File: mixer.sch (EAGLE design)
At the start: 49 parts, among them U1 MAX5419LETA+, U2 MAX5419LETA+, X1 OPAMP, X10 OPAMP, X3 OPAMP, X5 OPAMP, X6 OPAMP, X7 OPAMP, X8 OPAMP, X9 OPAMP

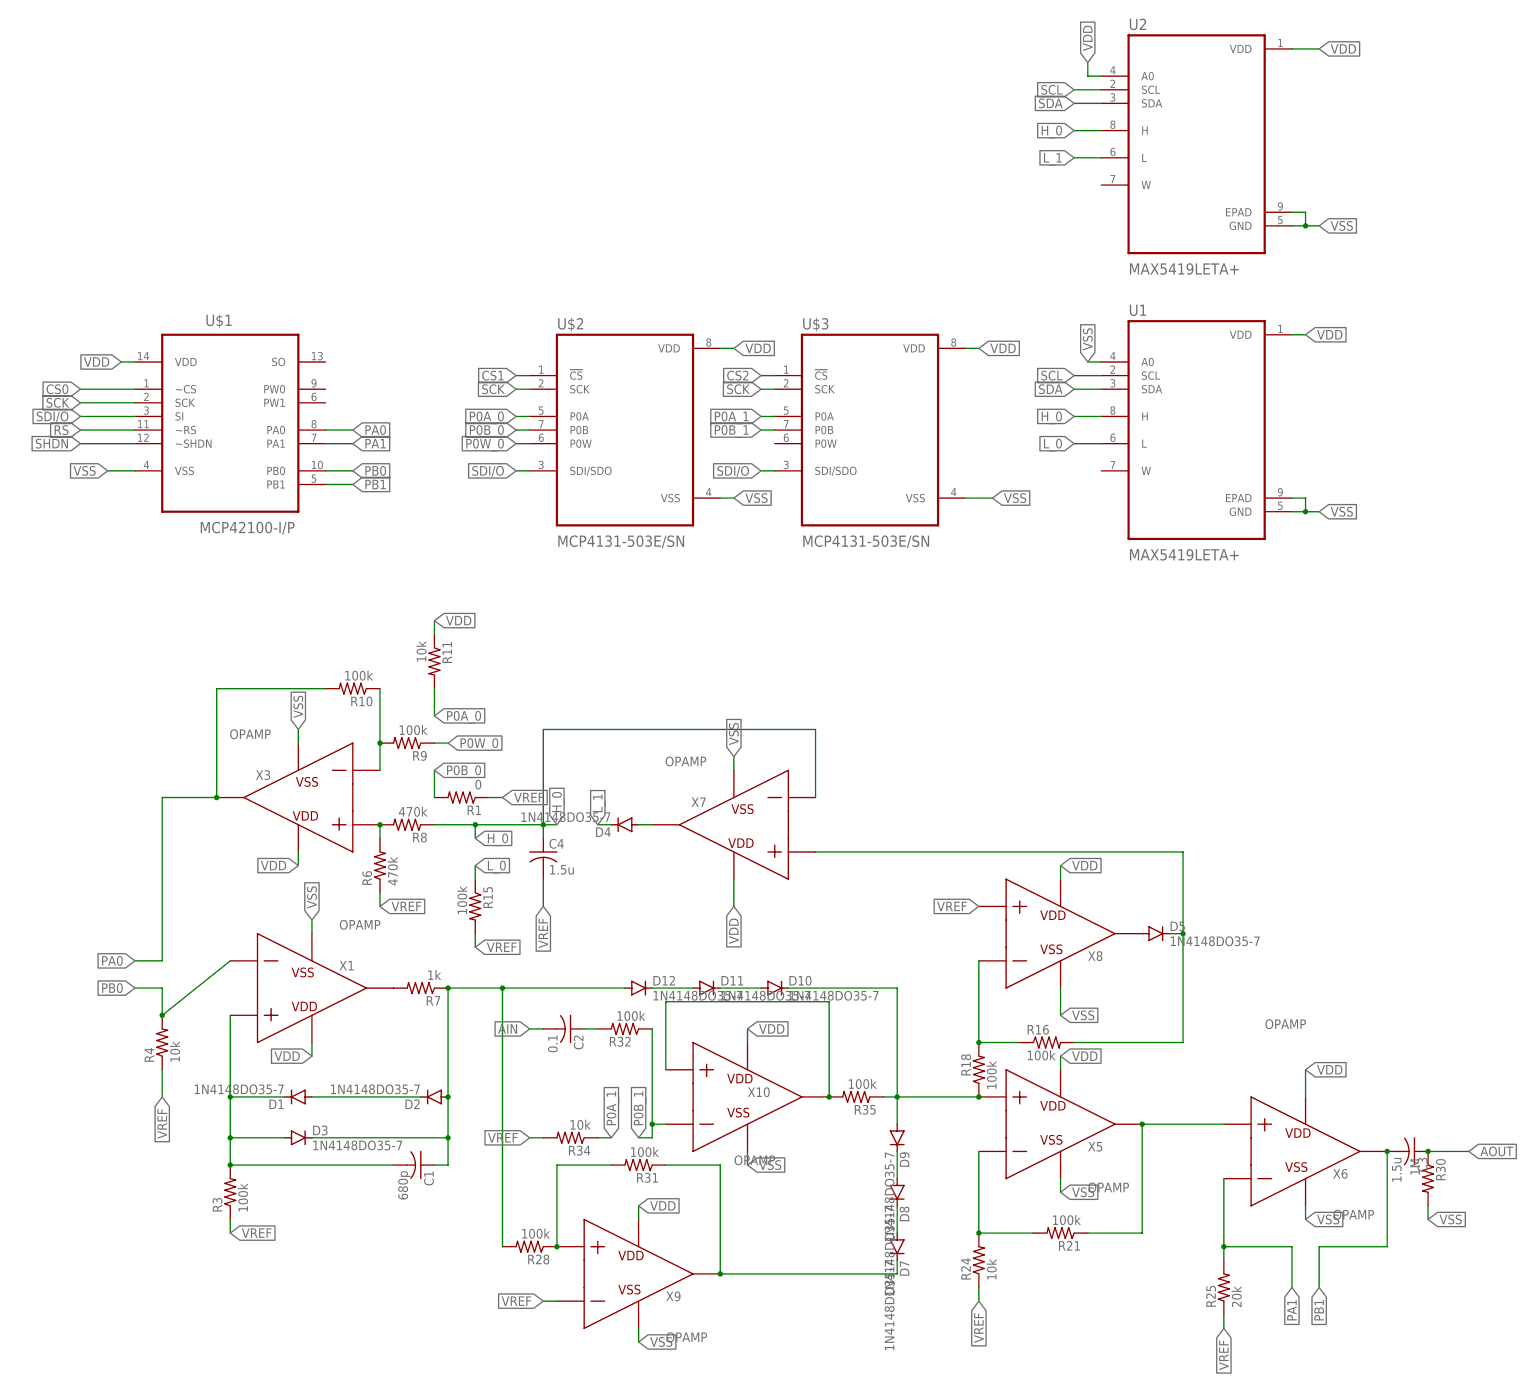
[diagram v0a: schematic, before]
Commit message: update, split out into schematics for each component
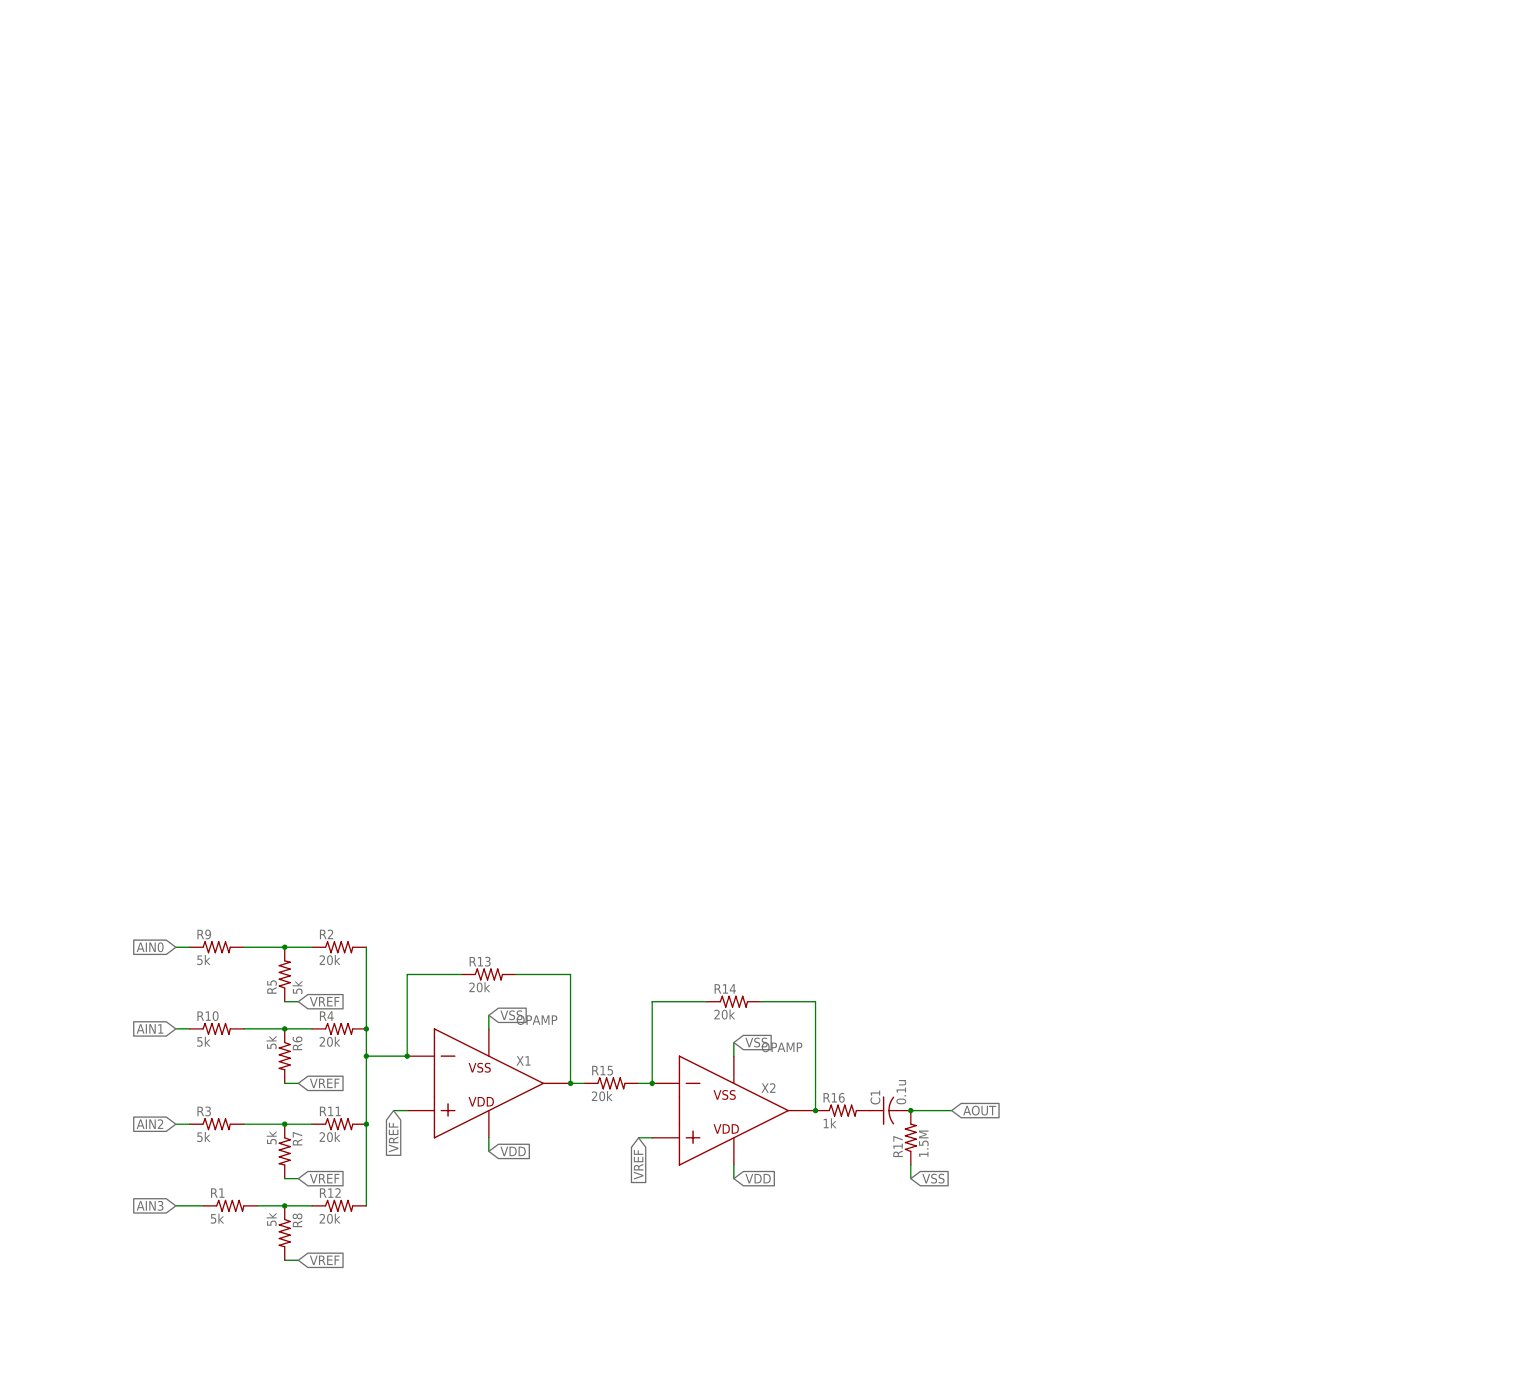
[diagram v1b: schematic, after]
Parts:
- removed C2: 0.1, rcl:C-US025-024X044
- removed C3, C4: 1.5u, rcl:C-US025-024X044
- removed D1, D10, D11, D12, D2, D3, D4, D5, D7, D8, D9: 1N4148DO35-7, diode:1N4148DO35-7
- removed R18, R21, R28, R31, R32, R35: 100k, rcl:R-US_0204/7
- removed R24, R34: 10k, rcl:R-US_0204/7
- removed R25: 20k, rcl:R-US_0204/7
- removed R30: 1M, rcl:R-US_0204/7
- removed U$1: MCP42100-I/P, MCP42100-I_P:MCP42100-I/P
- removed U$2, U$3: MCP4131-503E/SN, MCP4131-503E_SN:MCP4131-503E/SN
- removed U1, U2: MAX5419LETA+, MAX5419LETA_:MAX5419LETA+
- removed X10, X3, X5, X6, X7, X8, X9: OPAMP, ngspice-simulation:OPAMP
- added R12, R13, R14, R2: 20k, rcl:R-US_0204/7
- added R17: 1.5M, rcl:R-US_0204/7
- added R5: 5k, rcl:R-US_0204/7
- added X2: OPAMP, ngspice-simulation:OPAMP
- C1: value 680p -> 0.1u
- R1: value 0 -> 5k
- R10, R3, R9: value 100k -> 5k
- R11, R4: value 10k -> 20k
- R15: value 100k -> 20k
- R16: value 100k -> 1k
- R6, R8: value 470k -> 5k
- R7: value 1k -> 5k
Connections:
- removed net AIN: C2.2
- removed net CS0: U$1.~CS
- removed net CS1: U$2.!CS
- removed net CS2: U$3.!CS
- removed net H_0: C4.1, R8.1, U1.H, U2.H, X7.N
- removed net L_0: R15.1, U1.L
- removed net L_1: D4.C, U2.L
- removed net N$18: R21.1, X5.VOUT, X6.P
- removed net N$19: R21.2, R24.2, X5.N
- removed net N$20: D1.A, D2.C
- removed net N$21: C1.1, D12.A, D2.A, D3.C, R28.2, R7.1
- removed net N$22: R28.1, R31.2, X9.P
- removed net N$23: D7.C, R31.1, X9.VOUT
- removed net N$24: D8.A, D9.C
- removed net N$25: D7.A, D8.C
- removed net N$26: D10.C, D9.A, R18.1, R35.1, X5.P
- removed net N$27: R35.2, X10.P, X10.VOUT
- removed net N$3: C1.2, D1.C, D3.A, R3.2, X1.P
- removed net N$30: C2.1, R32.2
- removed net N$31: D11.A, D12.C
- removed net N$32: D10.A, D11.C
- removed net N$33: D5.A, X8.VOUT
- removed net N$6: R6.2, R8.2, X3.P
- removed net N$7: R10.1, R9.2, X3.N
- removed net P0A_0: R11.2, U$2.P0A
- removed net P0A_1: R34.1, U$3.P0A
- removed net P0B_0: R1.2, U$2.P0B
- removed net P0B_1: R32.1, U$3.P0B, X10.N
- removed net P0W_0: R9.1, U$2.P0W
- removed net PA0: R10.2, U$1.PA0, X3.VOUT
- removed net PA1: R25.2, U$1.PA1, X6.N
- removed net PB0: R4.2, U$1.PB0, X1.N
- removed net PB1: C3.2, U$1.PB1, X6.VOUT
- removed net RS: U$1.~RS
- removed net SCK: U$1.SCK, U$2.SCK, U$3.SCK
- removed net SCL: U1.SCL, U2.SCL
- removed net SDA: U1.SDA, U2.SDA
- removed net SDI/O: U$1.SI, U$2.SDI/SDO, U$3.SDI/SDO
- removed net SHDN: U$1.~SHDN
- new net AIN0: R9.1
- new net AIN1: R10.1
- new net AIN2: R3.1
- new net AIN3: R1.1
- new net N$13: R2.1, R5.2, R9.2
- new net N$17: R10.2, R4.1, R6.1
- new net N$2: R14.2, R16.1, X2.VOUT
- new net N$4: R13.2, R15.1, X1.VOUT
- new net N$5: R14.1, R15.2, X2.N
- net AOUT: now also C1.2, R17.2; no longer C3.1, R30.1
- net N$1: now also C1.1, R16.2; no longer R7.2, X1.VOUT
- net N$14: now also R11.2, R12.2, R13.1, R2.2, R4.2, X1.N; no longer D4.A, X7.VOUT
- net N$15: now also R1.2, R12.1, R8.1; no longer D5.C, R16.2, X7.P
- net N$16: now also R11.1, R3.2, R7.1; no longer R16.1, R18.2, X8.N
- net VDD: now also X2.VDD; no longer R11.1, U$1.VDD, U$2.VDD, U$3.VDD, U1.VDD, U2.A0, U2.VDD, X10.VDD, X3.VDD, X5.VDD, X6.VDD, X7.VDD, X8.VDD, X9.VDD
- net VREF: now also R5.1, R6.2, R7.2, R8.2, X1.P, X2.P; no longer C4.2, R1.1, R15.2, R24.1, R25.1, R3.1, R34.2, R4.1, R6.1, X9.N
- net VSS: now also R17.1, X2.VSS; no longer R30.2, U$1.VSS, U$2.VSS, U$3.VSS, U1.A0, U1.EPAD, U1.GND, U2.EPAD, U2.GND, X10.VSS, X3.VSS, X5.VSS, X6.VSS, X7.VSS, X8.VSS, X9.VSS
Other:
- moved on the sheet: C1, R1, R10, R11, R15, R16, R3, R4, R6, R7, R8, R9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

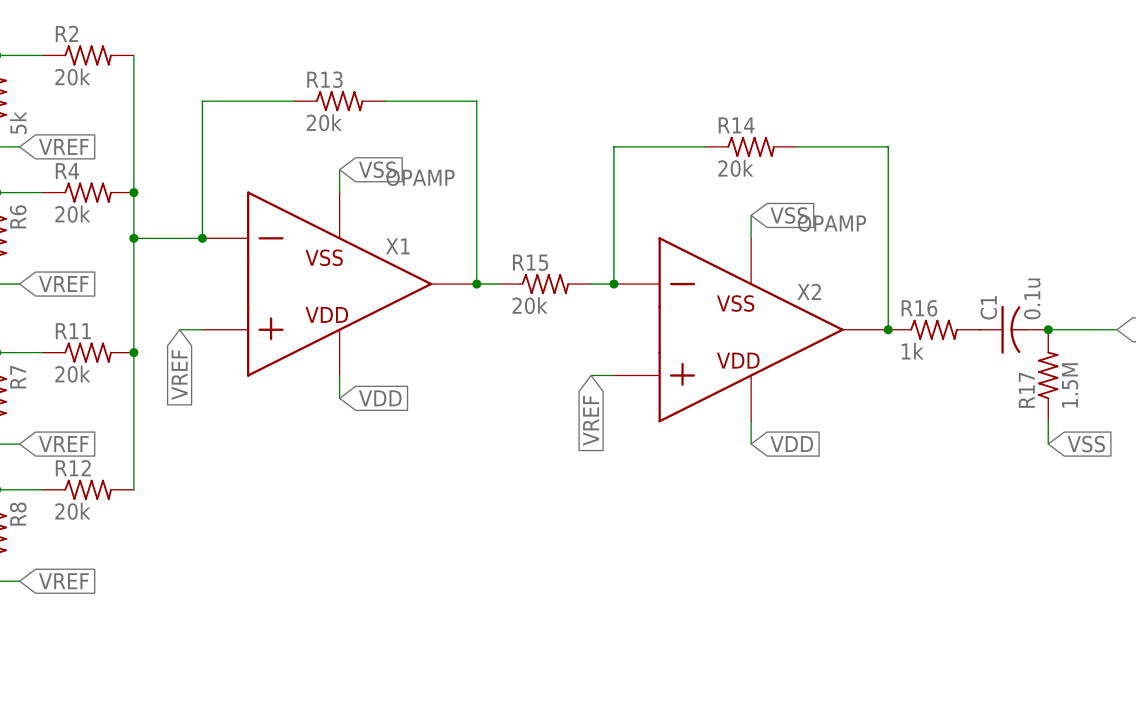
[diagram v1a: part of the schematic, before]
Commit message: rm cache files, add boards for components
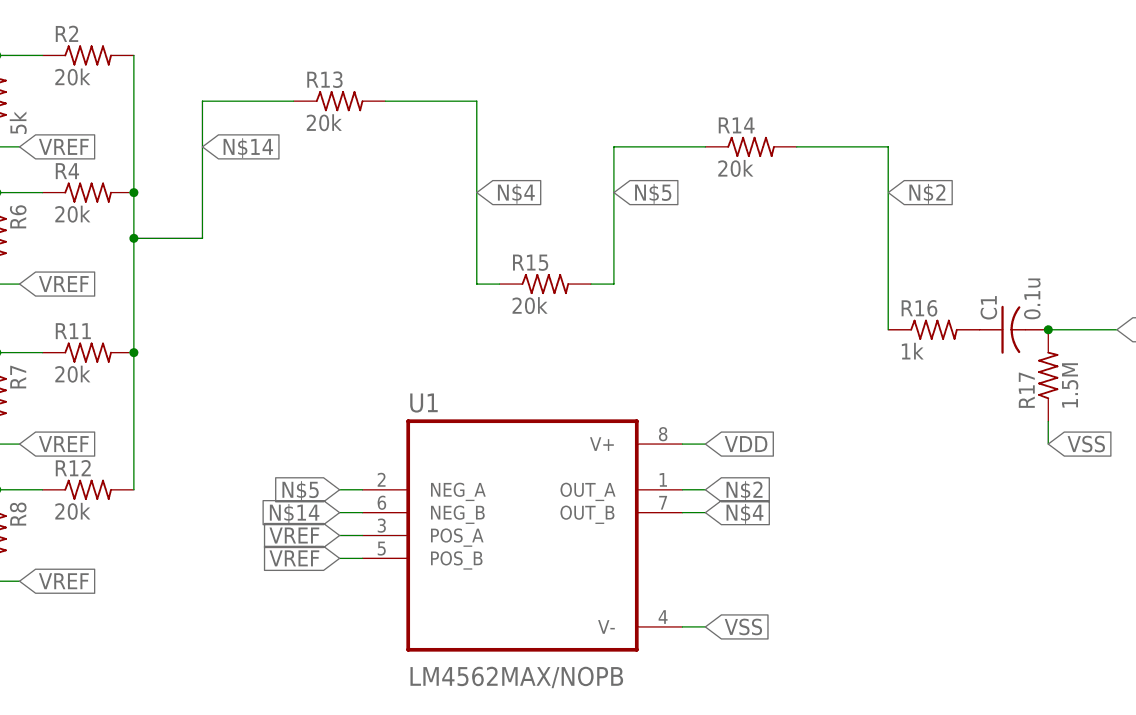
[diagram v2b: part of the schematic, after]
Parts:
- removed X1, X2: OPAMP, ngspice-simulation:OPAMP
- added U1: LM4562MAX/NOPB, LM4562MAX_NOPB:LM4562MAX/NOPB
- C1: device rcl:C-US025-024X044 -> rcl:C-USC0402
- R1, R10, R11, R12, R13, R14, R15, R16, R17, R2, R3, R4, R5, R6, R7, R8, R9: device rcl:R-US_0204/7 -> rcl:R-US_R0402
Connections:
- net N$14: now also U1.NEG_B; no longer X1.N
- net N$2: now also U1.OUT_A; no longer X2.VOUT
- net N$4: now also U1.OUT_B; no longer X1.VOUT
- net N$5: now also U1.NEG_A; no longer X2.N
- net VDD: now also U1.V+; no longer X1.VDD, X2.VDD
- net VREF: now also U1.POS_A, U1.POS_B; no longer X1.P, X2.P
- net VSS: now also U1.V-; no longer X1.VSS, X2.VSS

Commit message: corrections
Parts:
- removed R17: 1.5M, rcl:R-US_R0402
- added AOUT, GND: (no value), wirepad:SMD5
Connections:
- removed net VSS: R17.1, U1.V-
- new net GND: GND.P, U1.V-
- net AOUT: now also AOUT.P; no longer R17.2
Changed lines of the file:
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@@
 <class number="0" name="default" width="0" drill="0">
-</class>
-<class number="1" name="POWER" width="0.508" drill="0.508">
-<clearance class="1" value="0.254"/>
-</class>
-<class number="2" name="GND" width="0.508" drill="0.508">
-<clearance class="2" value="0.254"/>
-</class>
-<class number="3" name="DIGITAL" width="0.2032" drill="0.508">
-<clearance class="3" value="0.254"/>
-</class>
-<class number="4" name="ANALOG" width="0.508" drill="0.508">
-<clearance class="4" value="0.254"/>
 </class>
 </classes>
@@
 <part name="R15" library="rcl" library_urn="urn:adsk.eagle:library:334" deviceset="R-US_" device="R0402" package3d_urn="urn:adsk.eagle:package:23547/3" value="20k"/>
 <part name="R16" library="rcl" library_urn="urn:adsk.eagle:library:334" deviceset="R-US_" device="R0402" package3d_urn="urn:adsk.eagle:package:23547/3" value="1k"/>
-<part name="R17" library="rcl" library_urn="urn:adsk.eagle:library:334" deviceset="R-US_" device="R0402" package3d_urn="urn:adsk.eagle:package:23547/3" value="1.5M"/>
 <part name="C1" library="rcl" library_urn="urn:adsk.eagle:library:334" deviceset="C-US" device="C0402" package3d_urn="urn:adsk.eagle:package:23626/2" value="0.1u"/>
 <part name="U1" library="LM4562MAX_NOPB" deviceset="LM4562MAX/NOPB" device=""/>
+<part name="GND" library="wirepad" library_urn="urn:adsk.eagle:library:412" deviceset="SMD5" device="" package3d_urn="urn:adsk.eagle:package:30841/1"/>
+<part name="AOUT" library="wirepad" library_urn="urn:adsk.eagle:library:412" deviceset="SMD5" device="" package3d_urn="urn:adsk.eagle:package:30841/1"/>
 </parts>
 <sheets>
@@
 <attribute name="VALUE" x="130.81" y="29.718" size="1.778" layer="96"/>
 </instance>
-<instance part="R17" gate="G$1" x="147.32" y="27.94" smashed="yes" rot="R90">
-<attribute name="NAME" x="145.8214" y="24.13" size="1.778" layer="95" rot="R90"/>
-<attribute name="VALUE" x="150.622" y="24.13" size="1.778" layer="96" rot="R90"/>
-</instance>
 <instance part="C1" gate="G$1" x="142.24" y="33.02" smashed="yes" rot="R90">
 <attribute name="NAME" x="141.605" y="34.036" size="1.778" layer="95" rot="R90"/>
@@
 <attribute name="NAME" x="76.2" y="23.86" size="2.0828" layer="95" ratio="10" rot="SR0"/>
 <attribute name="VALUE" x="76.2" y="-6.54" size="2.0828" layer="96" ratio="10" rot="SR0"/>
+</instance>
+<instance part="GND" gate="1" x="152.4" y="20.32" smashed="yes" rot="R180">
+<attribute name="NAME" x="153.543" y="18.4658" size="1.778" layer="95" rot="R180"/>
+<attribute name="VALUE" x="153.543" y="23.622" size="1.778" layer="96" rot="R180"/>
+</instance>
+<instance part="AOUT" gate="1" x="157.48" y="27.94" smashed="yes" rot="R180">
+<attribute name="NAME" x="158.623" y="26.0858" size="1.778" layer="95" rot="R180"/>
+<attribute name="VALUE" x="158.623" y="31.242" size="1.778" layer="96" rot="R180"/>
 </instance>
 </instances>
@@
 </busses>
 <nets>
-<net name="N$1" class="4">
+<net name="N$1" class="0">
 <segment>
 <pinref part="R16" gate="G$1" pin="2"/>
@@
 </segment>
 </net>
-<net name="N$2" class="4">
+<net name="N$2" class="0">
 <segment>
 <pinref part="R16" gate="G$1" pin="1"/>
@@
 </segment>
 </net>
-<net name="AOUT" class="4">
+<net name="AOUT" class="0">
 <segment>
 <pinref part="C1" gate="G$1" pin="2"/>
-<pinref part="R17" gate="G$1" pin="2"/>
 <wire x1="147.32" y1="33.02" x2="154.94" y2="33.02" width="0.1524" layer="91"/>
-<junction x="147.32" y="33.02"/>
 <label x="154.94" y="33.02" size="1.778" layer="95" xref="yes"/>
-</segment>
-</net>
-<net name="N$4" class="4">
+<pinref part="AOUT" gate="1" pin="P"/>
+<wire x1="154.94" y1="33.02" x2="154.94" y2="27.94" width="0.1524" layer="91"/>
+</segment>
+</net>
+<net name="N$4" class="0">
 <segment>
 <pinref part="R15" gate="G$1" pin="1"/>
@@
 </segment>
 </net>
-<net name="N$5" class="4">
+<net name="N$5" class="0">
 <segment>
 <pinref part="R15" gate="G$1" pin="2"/>
@@
 </segment>
 </net>
-<net name="VSS" class="4">
-<segment>
-<pinref part="R17" gate="G$1" pin="1"/>
-<wire x1="147.32" y1="22.86" x2="147.32" y2="20.32" width="0.1524" layer="91"/>
-<label x="147.32" y="20.32" size="1.778" layer="95" xref="yes"/>
-</segment>
+<net name="GND" class="0">
 <segment>
 <pinref part="U1" gate="A" pin="V-"/>
@@
 <label x="109.22" y="0" size="1.778" layer="95" xref="yes"/>
 </segment>
-</net>
-<net name="VDD" class="4">
+<segment>
+<pinref part="GND" gate="1" pin="P"/>
+<wire x1="149.86" y1="20.32" x2="144.78" y2="20.32" width="0.1524" layer="91"/>
+<label x="144.78" y="20.32" size="1.778" layer="95" rot="R180" xref="yes"/>
+</segment>
+</net>
+<net name="VDD" class="0">
 <segment>
 <pinref part="U1" gate="A" pin="V+"/>
@@
 </segment>
 </net>
-<net name="N$13" class="4">
+<net name="N$13" class="0">
 <segment>
 <pinref part="R9" gate="G$1" pin="2"/>
@@
 </segment>
 </net>
-<net name="N$14" class="4">
+<net name="N$14" class="0">
 <segment>
 <pinref part="R2" gate="G$1" pin="2"/>
@@
 </segment>
 </net>
-<net name="N$15" class="4">
+<net name="N$15" class="0">
 <segment>
 <pinref part="R8" gate="G$1" pin="1"/>
@@
 </segment>
 </net>
-<net name="N$16" class="4">
+<net name="N$16" class="0">
 <segment>
 <pinref part="R11" gate="G$1" pin="1"/>
@@
 </segment>
 </net>
-<net name="N$17" class="4">
+<net name="N$17" class="0">
 <segment>
 <pinref part="R6" gate="G$1" pin="1"/>
@@
 </segment>
 </net>
-<net name="AIN0" class="4">
+<net name="AIN0" class="0">
 <segment>
 <pinref part="R9" gate="G$1" pin="1"/>
@@
 </segment>
 </net>
-<net name="AIN1" class="4">
+<net name="AIN1" class="0">
 <segment>
 <pinref part="R10" gate="G$1" pin="1"/>
@@
 </segment>
 </net>
-<net name="AIN2" class="4">
+<net name="AIN2" class="0">
 <segment>
 <pinref part="R3" gate="G$1" pin="1"/>
@@
 </segment>
 </net>
-<net name="AIN3" class="4">
+<net name="AIN3" class="0">
 <segment>
 <pinref part="R1" gate="G$1" pin="1"/>
@@
 </segment>
 </net>
-<net name="VREF" class="4">
+<net name="VREF" class="0">
 <segment>
 <pinref part="R5" gate="G$1" pin="1"/>
